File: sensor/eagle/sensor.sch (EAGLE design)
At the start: 18 parts

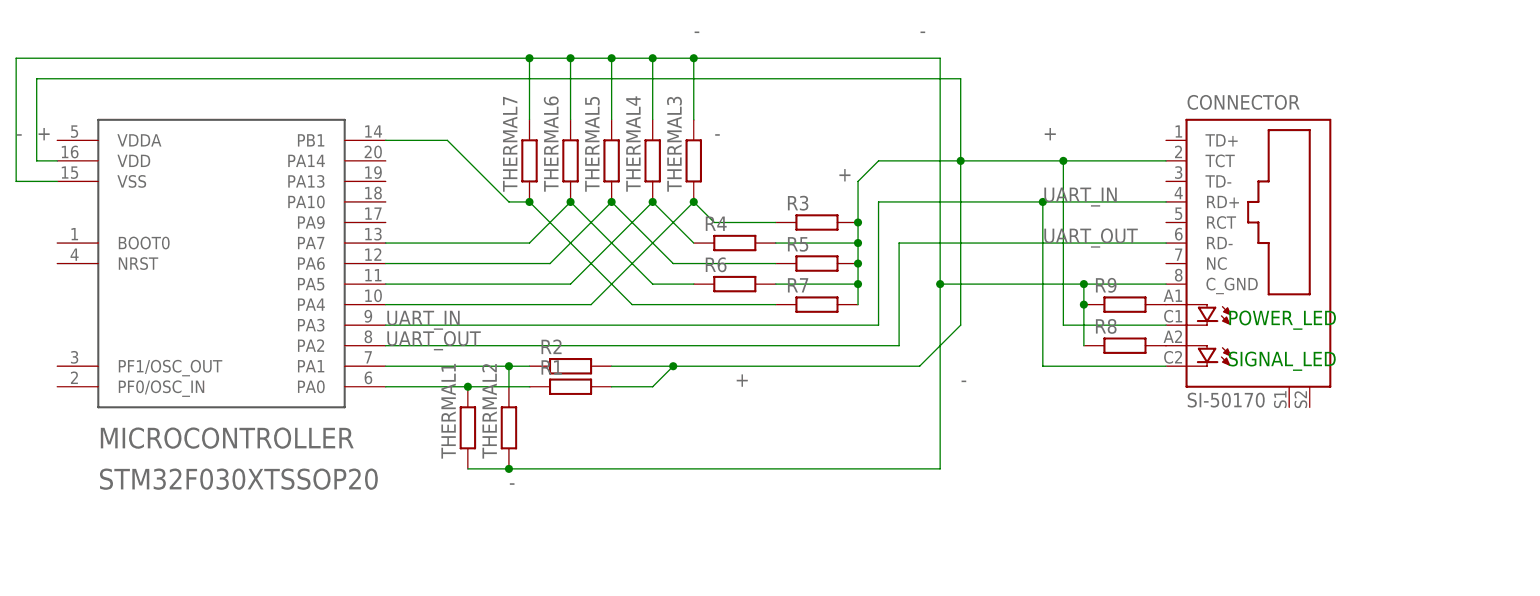
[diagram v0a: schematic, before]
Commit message: Updated sensor's scheme, colletor's photo and README.md
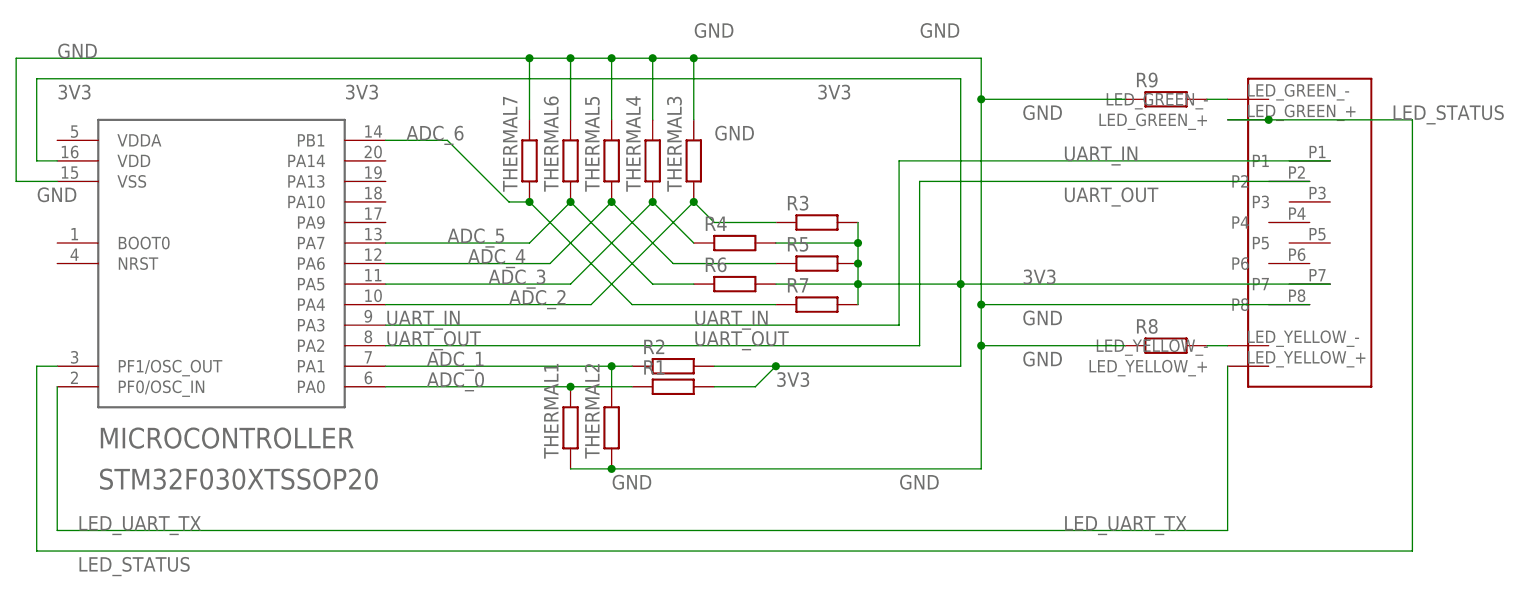
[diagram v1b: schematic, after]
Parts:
- removed CONNECTOR: SI-50170, con-stewart:SI-50170
- added U$1: RJHSE-5481_(RJ45), ut-connectors:RJHSE-5481_(RJ45)
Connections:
- net N$1 renamed ADC_2
- net N$3 renamed ADC_3
- net N$5 renamed ADC_0
- net N$6 renamed ADC_1
- net N$7 renamed ADC_4
- net N$8 renamed ADC_5
- net N$9 renamed ADC_6
- removed net +: CONNECTOR.C, CONNECTOR.TCT, MICROCONTROLLER.VDD, R1.2, R2.2, R3.2, R4.2, R5.2, R6.2, R7.2
- removed net -: CONNECTOR.C_GND, MICROCONTROLLER.VSS, R8.1, R9.1, THERMAL1.1, THERMAL2.1, THERMAL3.2, THERMAL4.2, THERMAL5.2, THERMAL6.2, THERMAL7.2
- removed net N$4: CONNECTOR.A, R9.2
- new net 3V3: MICROCONTROLLER.VDD, R1.2, R2.2, R3.2, R4.2, R5.2, R6.2, R7.2, U$1.P7
- new net GND: MICROCONTROLLER.VSS, R8.1, R9.1, THERMAL1.1, THERMAL2.1, THERMAL3.2, THERMAL4.2, THERMAL5.2, THERMAL6.2, THERMAL7.2, U$1.P8
- new net LED_STATUS: MICROCONTROLLER.PF1/OSC_OUT, U$1.LED_GREEN_+
- new net LED_UART_TX: MICROCONTROLLER.PF0/OSC_IN
- new net N$1: R9.2
- net N$2: no longer CONNECTOR.A1
- net UART_IN: now also U$1.P1; no longer CONNECTOR.C1, CONNECTOR.RD+
- net UART_OUT: now also U$1.P2; no longer CONNECTOR.RD-
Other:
- note removed: "POWER_LED"
- note removed: "SIGNAL_LED"
- moved on the sheet: R1, R2, R8, R9, THERMAL1, THERMAL2
